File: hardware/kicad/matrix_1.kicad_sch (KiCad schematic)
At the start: 166 parts, among them U5 IS31FL3741A

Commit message: Update KiCAD files
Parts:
- removed R20, R21: 4.7k, Resistor_SMD:R_0402_1005Metric, symbol Device:R_Small_US

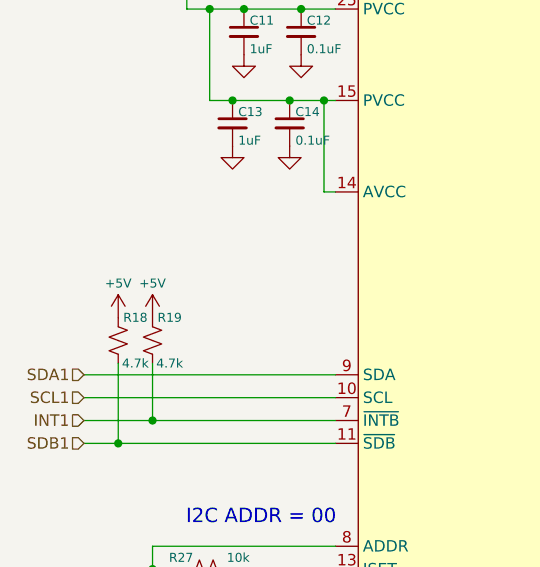
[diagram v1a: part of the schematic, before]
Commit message: Update KiCAD files
correct files this time :)
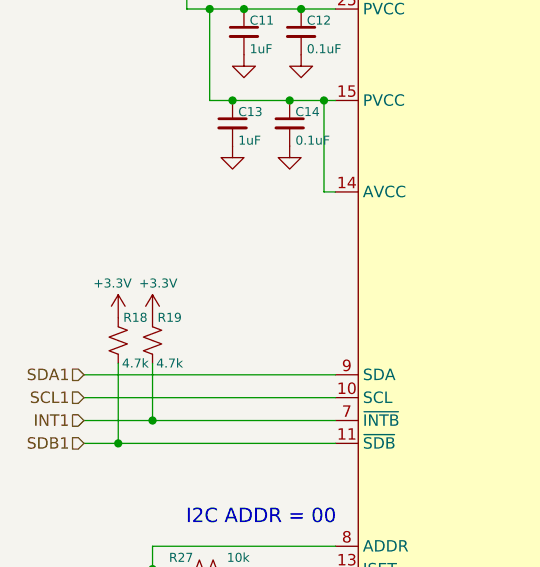
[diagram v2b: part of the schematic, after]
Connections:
- net +5V: no longer R18.1, R19.1
- new net +3.3V: R18.1, R19.1
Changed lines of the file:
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@@
 	)
 	(symbol
+		(lib_id "power:+3.3V")
+		(at 36.83 74.93 0)
+		(unit 1)
+		(exclude_from_sim no)
+		(in_bom yes)
+		(on_board yes)
+		(dnp no)
+		(property "Reference" "#PWR032"
+			(at 36.83 78.74 0)
+			(effects
+				(font
+					(size 1.27 1.27)
+				)
+				(hide yes)
+			)
+		)
+		(property "Value" "+3.3V"
+			(at 36.195 71.12 0)
+			(effects
+				(font
+					(size 1 1)
+				)
+			)
+		)
+		(property "Footprint" ""
+			(at 36.83 74.93 0)
+			(effects
+				(font
+					(size 1.27 1.27)
+				)
+				(hide yes)
+			)
+		)
+		(property "Datasheet" ""
+			(at 36.83 74.93 0)
+			(effects
+				(font
+					(size 1.27 1.27)
+				)
+				(hide yes)
+			)
+		)
+		(property "Description" "Power symbol creates a global label with name \"+3.3V\""
+			(at 36.83 74.93 0)
+			(effects
+				(font
+					(size 1.27 1.27)
+				)
+				(hide yes)
+			)
+		)
+		(pin "1"
+		)
+		(instances
+			(project "traffic_paradise"
+				(path "/911505fc-874d-4338-908e-12054bdd5112/11297df2-e2a9-48ca-8c4a-a4275dbea0eb"
+					(reference "#PWR032")
+					(unit 1)
+				)
+			)
+		)
+	)
+	(symbol
+		(lib_id "power:+3.3V")
+		(at 40.64 74.93 0)
+		(unit 1)
+		(exclude_from_sim no)
+		(in_bom yes)
+		(on_board yes)
+		(dnp no)
+		(property "Reference" "#PWR035"
+			(at 40.64 78.74 0)
+			(effects
+				(font
+					(size 1.27 1.27)
+				)
+				(hide yes)
+			)
+		)
+		(property "Value" "+3.3V"
+			(at 41.275 71.12 0)
+			(effects
+				(font
+					(size 1 1)
+				)
+			)
+		)
+		(property "Footprint" ""
+			(at 40.64 74.93 0)
+			(effects
+				(font
+					(size 1.27 1.27)
+				)
+				(hide yes)
+			)
+		)
+		(property "Datasheet" ""
+			(at 40.64 74.93 0)
+			(effects
+				(font
+					(size 1.27 1.27)
+				)
+				(hide yes)
+			)
+		)
+		(property "Description" "Power symbol creates a global label with name \"+3.3V\""
+			(at 40.64 74.93 0)
+			(effects
+				(font
+					(size 1.27 1.27)
+				)
+				(hide yes)
+			)
+		)
+		(pin "1"
+		)
+		(instances
+			(project "traffic_paradise"
+				(path "/911505fc-874d-4338-908e-12054bdd5112/11297df2-e2a9-48ca-8c4a-a4275dbea0eb"
+					(reference "#PWR035")
+					(unit 1)
+				)
+			)
+		)
+	)
+	(symbol
 		(lib_id "Device:LED_RABG")
 		(at 241.3 209.55 0)
@@
 	)
 	(symbol
-		(lib_id "power:+5V")
-		(at 36.83 74.93 0)
-		(unit 1)
-		(exclude_from_sim no)
-		(in_bom yes)
-		(on_board yes)
-		(dnp no)
-		(property "Reference" "#PWR032"
-			(at 36.83 78.74 0)
-			(effects
-				(font
-					(size 1.27 1.27)
-				)
-				(hide yes)
-			)
-		)
-		(property "Value" "+5V"
-			(at 36.83 71.12 0)
-			(effects
-				(font
-					(size 1 1)
-				)
-			)
-		)
-		(property "Footprint" ""
-			(at 36.83 74.93 0)
-			(effects
-				(font
-					(size 1.27 1.27)
-				)
-				(hide yes)
-			)
-		)
-		(property "Datasheet" ""
-			(at 36.83 74.93 0)
-			(effects
-				(font
-					(size 1.27 1.27)
-				)
-				(hide yes)
-			)
-		)
-		(property "Description" "Power symbol creates a global label with name \"+5V\""
-			(at 36.83 74.93 0)
-			(effects
-				(font
-					(size 1.27 1.27)
-				)
-				(hide yes)
-			)
-		)
-		(pin "1"
-		)
-		(instances
-			(project "v0"
-				(path "/911505fc-874d-4338-908e-12054bdd5112/11297df2-e2a9-48ca-8c4a-a4275dbea0eb"
-					(reference "#PWR032")
-					(unit 1)
-				)
-			)
-		)
-	)
-	(symbol
 		(lib_id "Device:R_Small_US")
 		(at 137.16 77.47 90)
@@
 					(unit 1)
 				)
-			)
-		)
-	)
-	(symbol
-		(lib_id "power:+5V")
-		(at 40.64 74.93 0)
-		(unit 1)
-		(exclude_from_sim no)
-		(in_bom yes)
-		(on_board yes)
-		(dnp no)
-		(property "Reference" "#PWR035"
-			(at 40.64 78.74 0)
-			(effects
-				(font
-					(size 1.27 1.27)
-				)
-				(hide yes)
-			)
-		)
-		(property "Value" "+5V"
-			(at 40.64 71.12 0)
-			(effects
-				(font
-					(size 1 1)
-				)
-			)
-		)
-		(property "Footprint" ""
-			(at 40.64 74.93 0)
-			(effects
-				(font
-					(size 1.27 1.27)
-				)
-				(hide yes)
-			)
-		)
-		(property "Datasheet" ""
-			(at 40.64 74.93 0)
-			(effects
-				(font
-					(size 1.27 1.27)
-				)
-				(hide yes)
-			)
-		)
-		(property "Description" "Power symbol creates a global label with name \"+5V\""
-			(at 40.64 74.93 0)
-			(effects
-				(font
-					(size 1.27 1.27)
-				)
-				(hide yes)
-			)
-		)
-		(pin "1"
-		)
-		(instances
-			(project "v0"
-				(path "/911505fc-874d-4338-908e-12054bdd5112/11297df2-e2a9-48ca-8c4a-a4275dbea0eb"
-					(reference "#PWR035")
-					(unit 1)
-				)

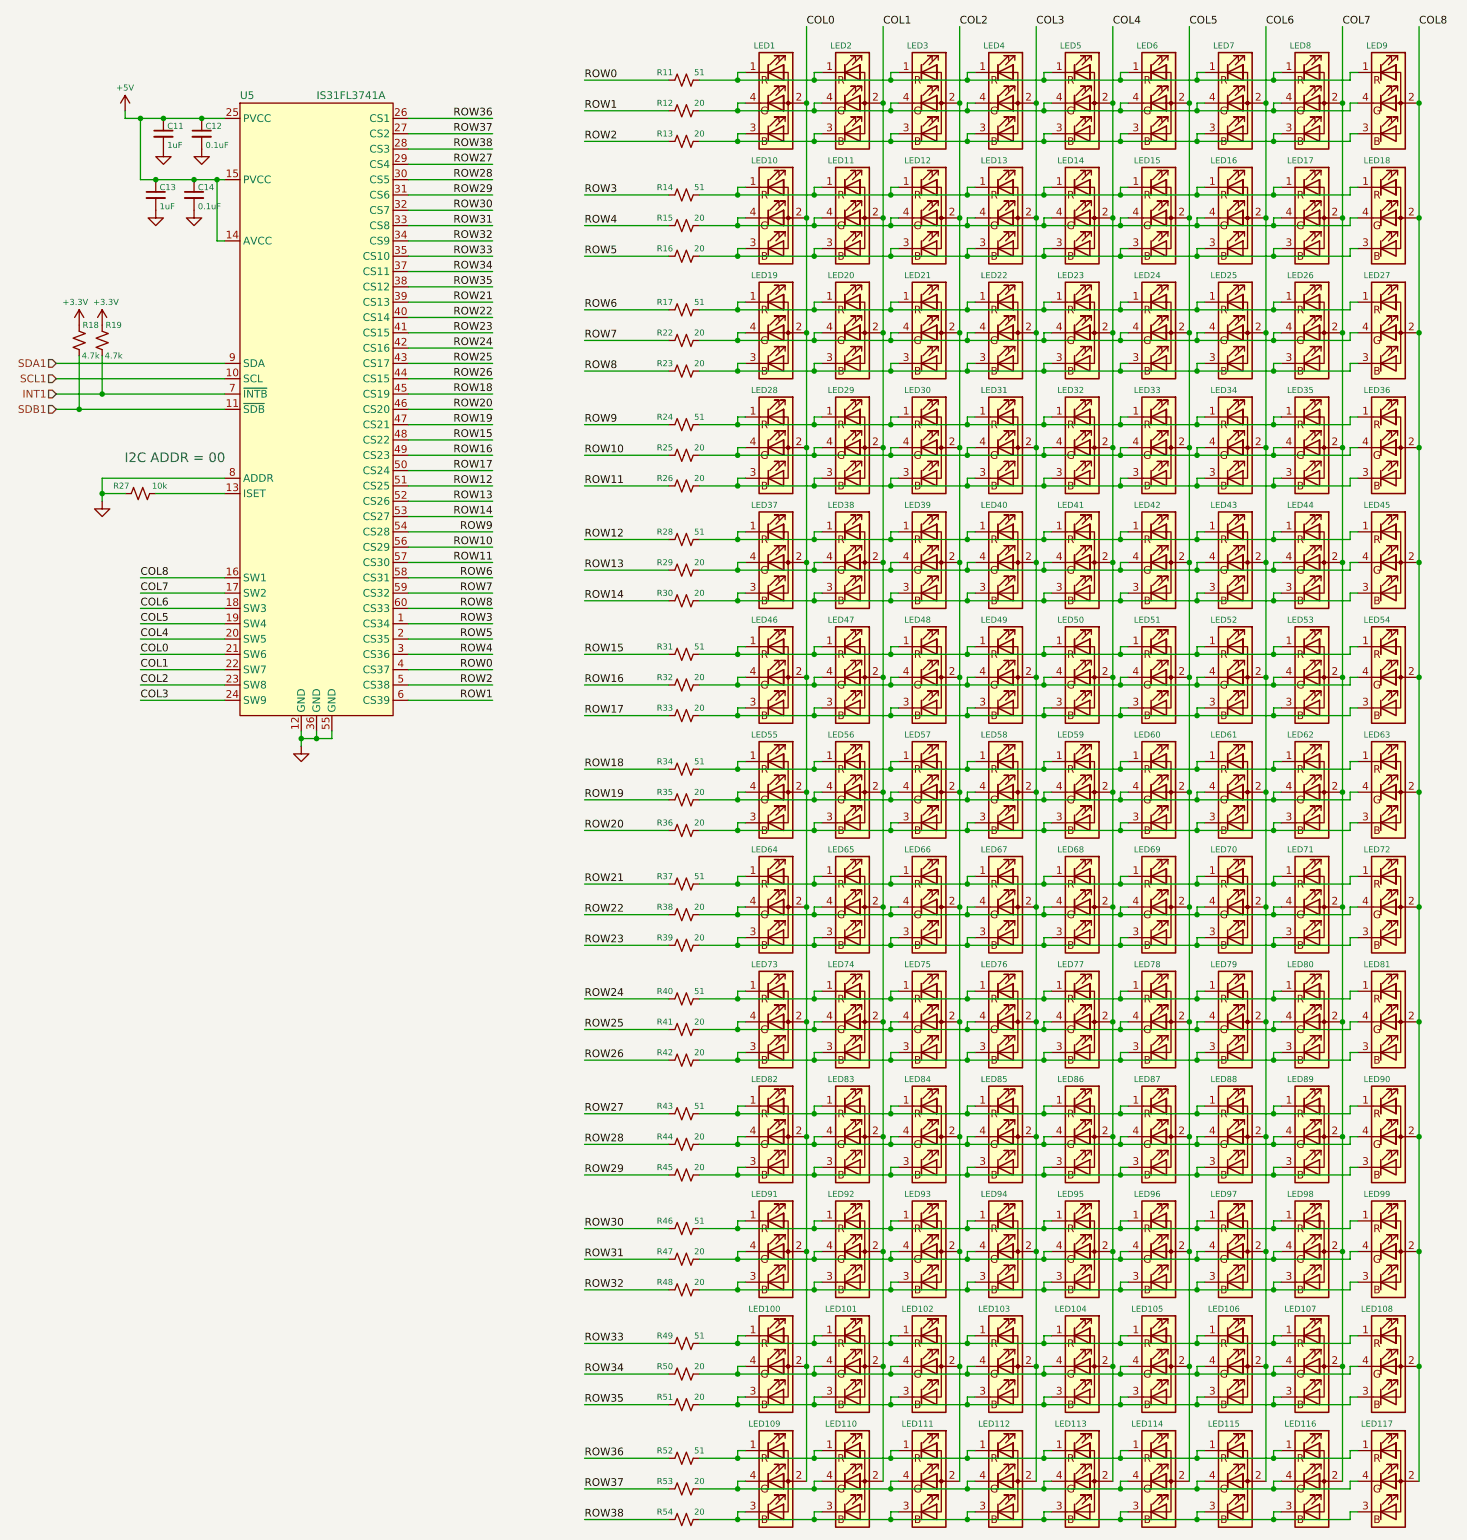
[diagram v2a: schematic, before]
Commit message: add and route matrix 4
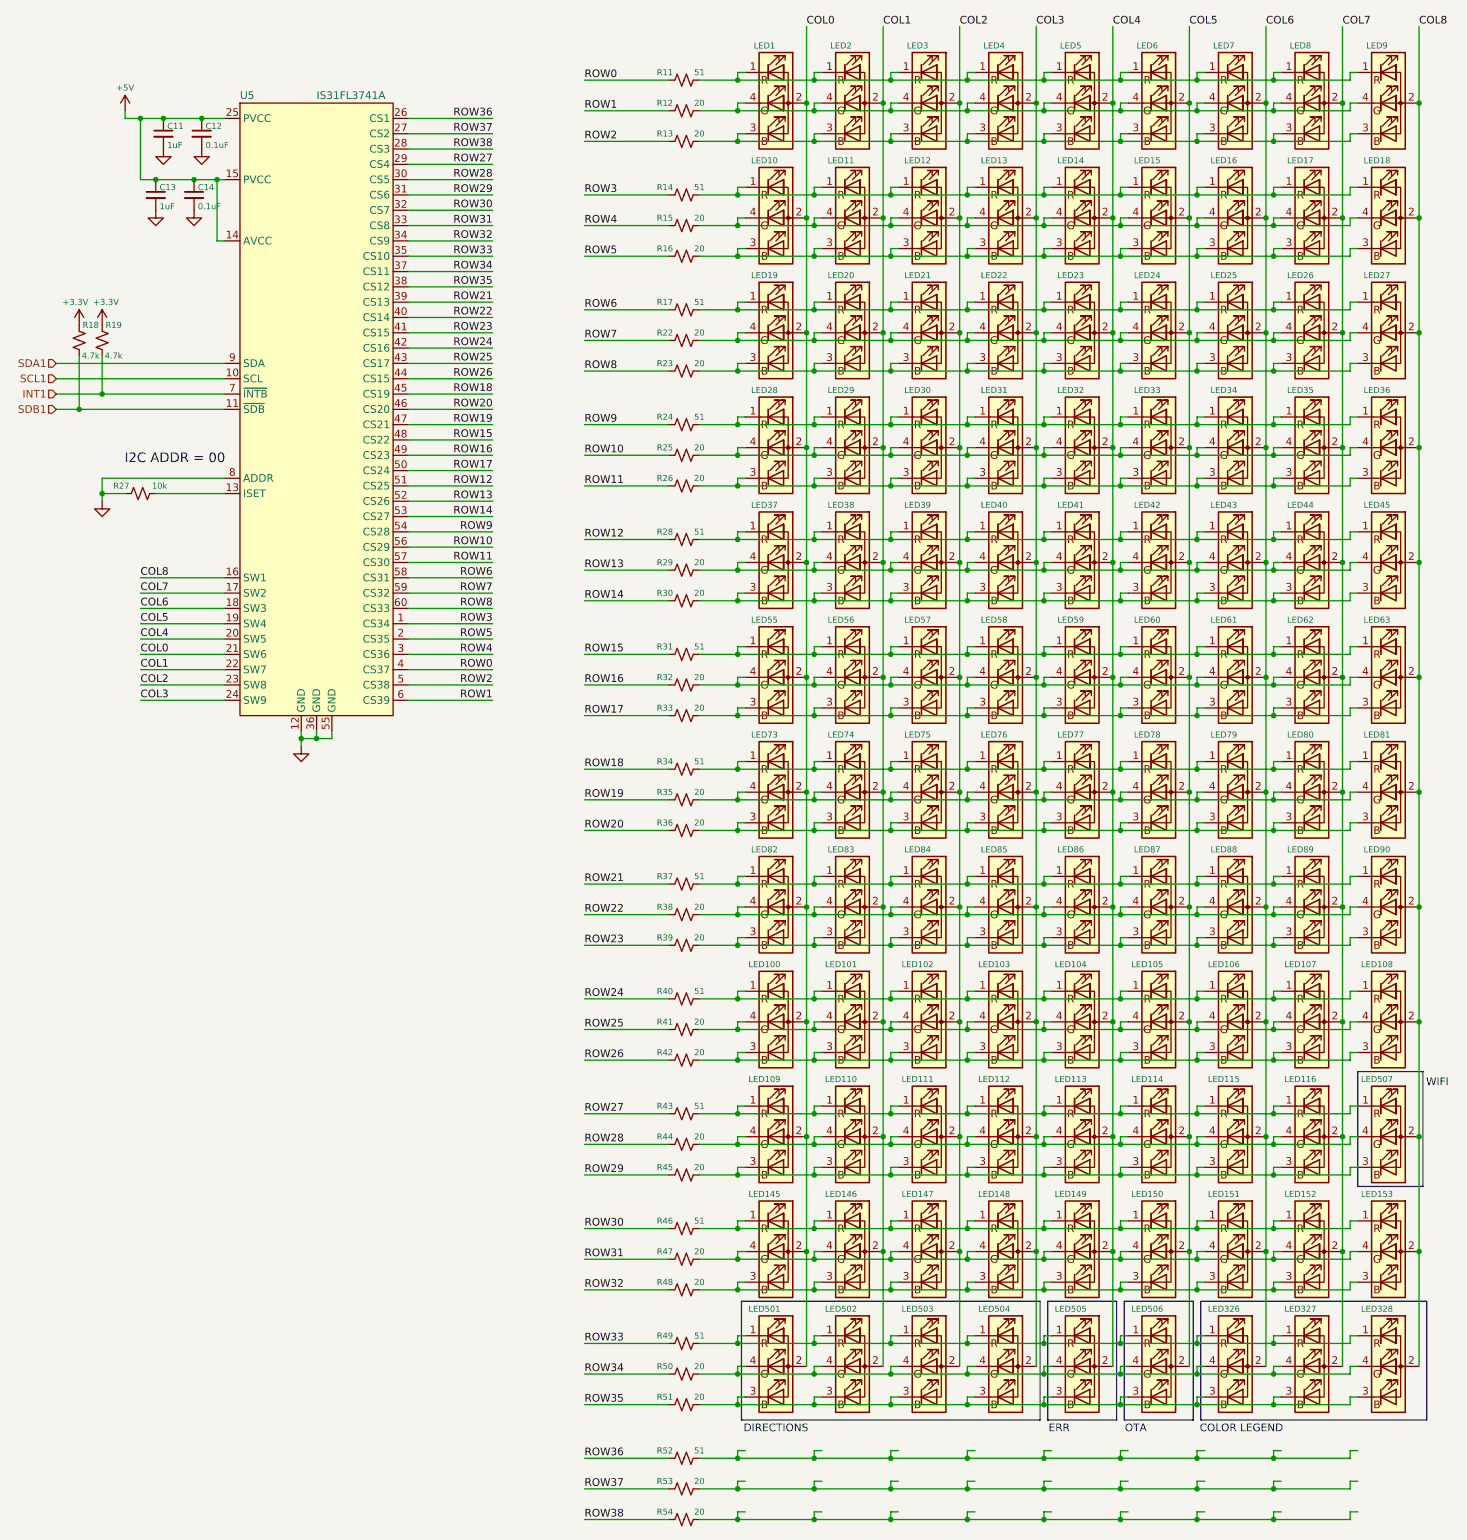
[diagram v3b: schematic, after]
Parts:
- removed LED117, LED46, LED47, LED48, LED49, LED50, LED51, LED52, LED53, LED54, LED64, LED65, LED66, LED67, LED68, LED69, LED70, LED71, LED72, LED91, LED92, LED93, LED94, LED95, LED96, LED97, LED98, LED99: LED_ARGB, map_lbr:LED_RGB_0606, symbol Device:LED_RABG
- added LED145, LED146, LED147, LED148, LED149, LED150, LED151, LED152, LED153, LED326, LED327, LED328, LED501, LED502, LED503, LED504, LED505, LED506, LED507: LED_ARGB, map_lbr:LED_RGB_0606, symbol Device:LED_RABG
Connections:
- net COL0: now also LED145.2 (A), LED501.2 (A)
- net COL1: now also LED146.2 (A), LED502.2 (A)
- net COL2: now also LED147.2 (A), LED503.2 (A)
- net COL3: now also LED148.2 (A), LED504.2 (A)
- net COL4: now also LED149.2 (A), LED505.2 (A)
- net COL5: now also LED150.2 (A), LED506.2 (A)
- net COL6: now also LED151.2 (A), LED326.2 (A)
- net COL7: now also LED152.2 (A), LED327.2 (A)
- net COL8: now also LED153.2 (A), LED328.2 (A), LED507.2 (A)
- net at LED109.1 (RK), LED110.1 (RK), LED111.1 (RK)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: now also R43.2, LED507.1 (RK); no longer R52.2
- net at LED109.3 (BK), LED110.3 (BK), LED111.3 (BK)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: now also R45.2, LED507.3 (BK); no longer R54.2
- net at LED109.4 (GK), LED110.4 (GK), LED111.4 (GK)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: now also R44.2, LED507.4 (GK); no longer R53.2
- net at R38.2: now also LED82.4 (GK), LED83.4 (GK), LED84.4 (GK), LED85.4 (GK), LED86.4 (GK), LED87.4 (GK), LED88.4 (GK), LED89.4 (GK), LED90.4 (GK)
- net at LED82.1 (RK), LED83.1 (RK), LED84.1 (RK)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: now also R37.2; no longer R43.2
- net at LED82.3 (BK), LED83.3 (BK), LED84.3 (BK)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: now also R39.2; no longer R45.2
- net at LED100.1 (RK), LED101.1 (RK), LED102.1 (RK)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: now also R40.2; no longer R49.2
- net at LED100.3 (BK), LED101.3 (BK), LED102.3 (BK)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: now also R42.2; no longer R51.2
- net at LED100.4 (GK), LED101.4 (GK), LED102.4 (GK)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: now also R41.2; no longer R50.2
- net at LED73.1 (RK), LED74.1 (RK), LED75.1 (RK)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: now also R34.2; no longer R40.2
- net at LED73.3 (BK), LED74.3 (BK), LED75.3 (BK)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: now also R36.2; no longer R42.2
- net at LED73.4 (GK), LED74.4 (GK), LED75.4 (GK)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: now also R35.2; no longer R41.2
- net at R46.2: now also LED145.1 (RK), LED146.1 (RK), LED147.1 (RK), LED148.1 (RK), LED149.1 (RK), LED150.1 (RK), LED151.1 (RK), LED152.1 (RK), LED153.1 (RK)
- net at R48.2: now also LED145.3 (BK), LED146.3 (BK), LED147.3 (BK), LED148.3 (BK), LED149.3 (BK), LED150.3 (BK), LED151.3 (BK), LED152.3 (BK), LED153.3 (BK)
- net at R47.2: now also LED145.4 (GK), LED146.4 (GK), LED147.4 (GK), LED148.4 (GK), LED149.4 (GK), LED150.4 (GK), LED151.4 (GK), LED152.4 (GK), LED153.4 (GK)
- net at R31.2: now also LED55.1 (RK), LED56.1 (RK), LED57.1 (RK), LED58.1 (RK), LED59.1 (RK), LED60.1 (RK), LED61.1 (RK), LED62.1 (RK), LED63.1 (RK)
- net at R33.2: now also LED55.3 (BK), LED56.3 (BK), LED57.3 (BK), LED58.3 (BK), LED59.3 (BK), LED60.3 (BK), LED61.3 (BK), LED62.3 (BK), LED63.3 (BK)
- net at R32.2: now also LED55.4 (GK), LED56.4 (GK), LED57.4 (GK), LED58.4 (GK), LED59.4 (GK), LED60.4 (GK), LED61.4 (GK), LED62.4 (GK), LED63.4 (GK)
- new net: LED326.1 (RK), LED327.1 (RK), LED328.1 (RK), LED501.1 (RK), LED502.1 (RK), LED503.1 (RK), LED504.1 (RK), LED505.1 (RK), LED506.1 (RK), R49.2
- new net: LED326.3 (BK), LED327.3 (BK), LED328.3 (BK), LED501.3 (BK), LED502.3 (BK), LED503.3 (BK), LED504.3 (BK), LED505.3 (BK), LED506.3 (BK), R51.2
- new net: LED326.4 (GK), LED327.4 (GK), LED328.4 (GK), LED501.4 (GK), LED502.4 (GK), LED503.4 (GK), LED504.4 (GK), LED505.4 (GK), LED506.4 (GK), R50.2
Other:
- note added: "COLOR LEGEND"
- note added: "DIRECTIONS"
- note added: "ERR"
- note added: "OTA"
- note added: "WIFI"
- moved on the sheet: LED100, LED101, LED102, LED103, LED104, LED105, LED106, LED107, LED108, LED109, LED110, LED111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
